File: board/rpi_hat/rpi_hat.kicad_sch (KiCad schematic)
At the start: 9 parts, among them J1 DB9_Male, J2 DB9_Male, J3 Raspberry_Pi_2_3

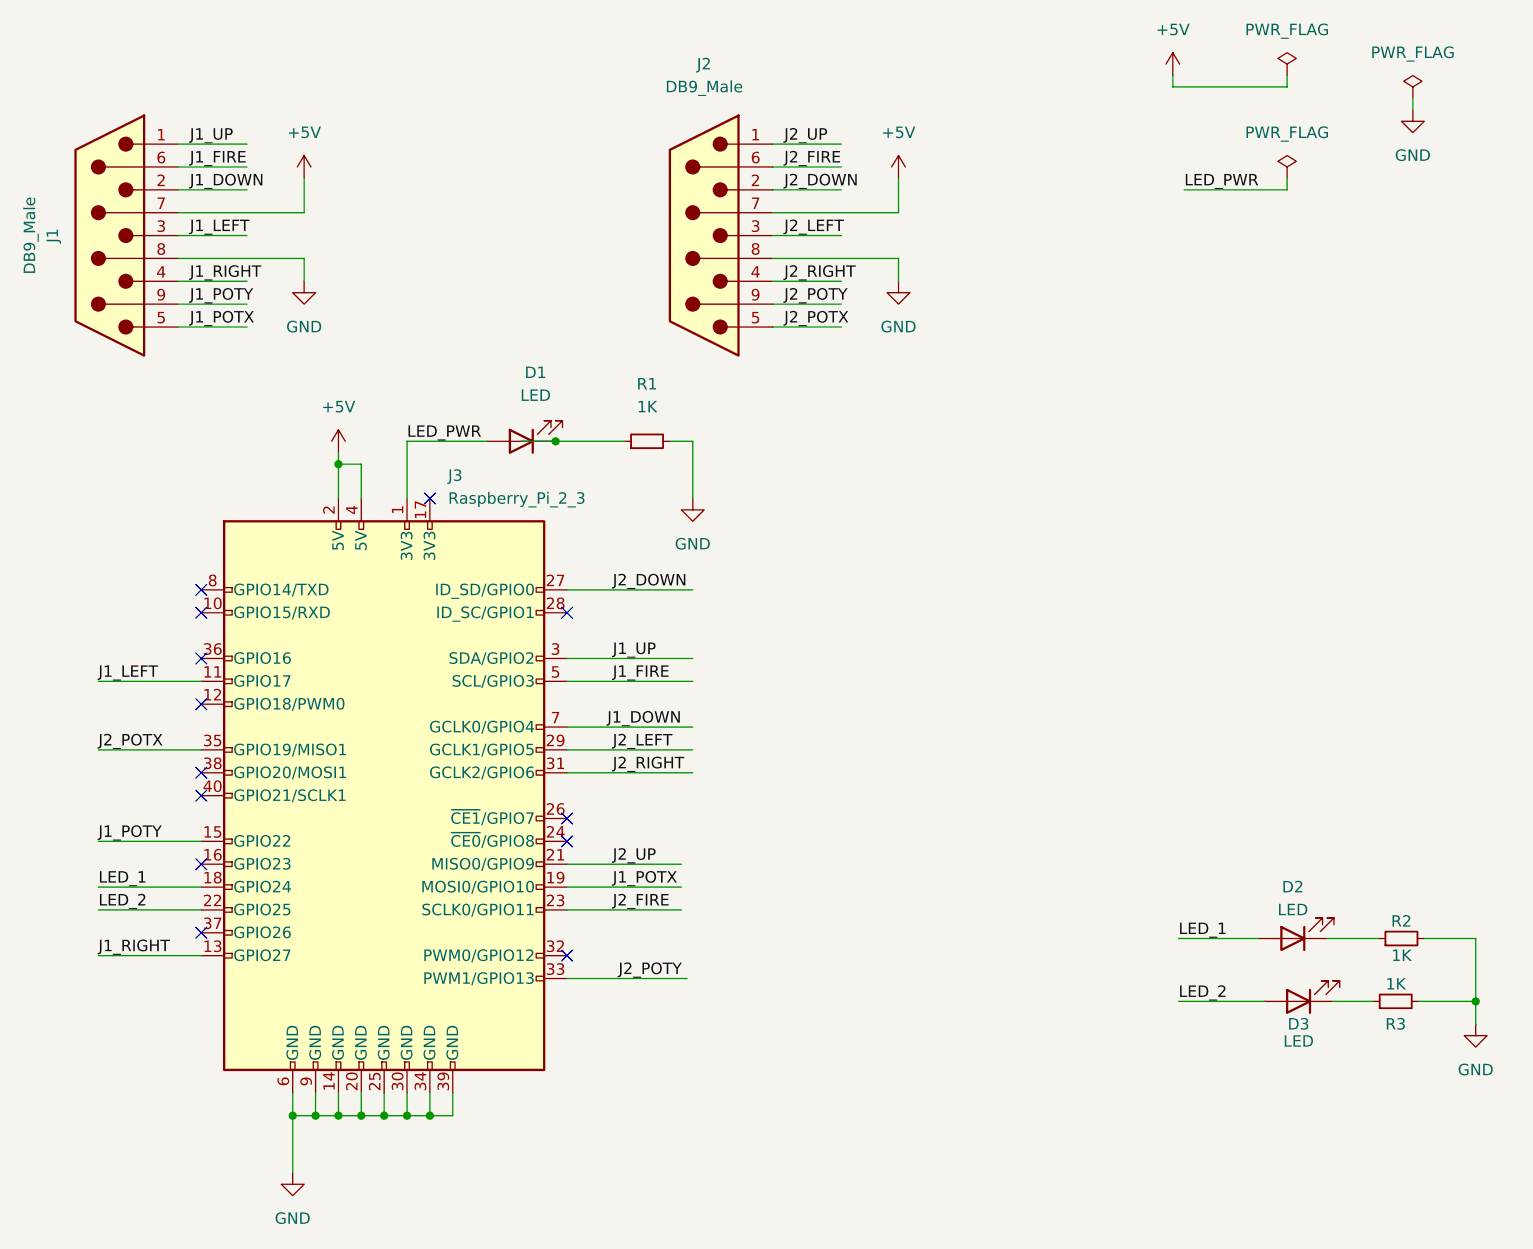
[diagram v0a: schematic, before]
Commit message: rpi hat: rev A
Routing re done to make it easier to use
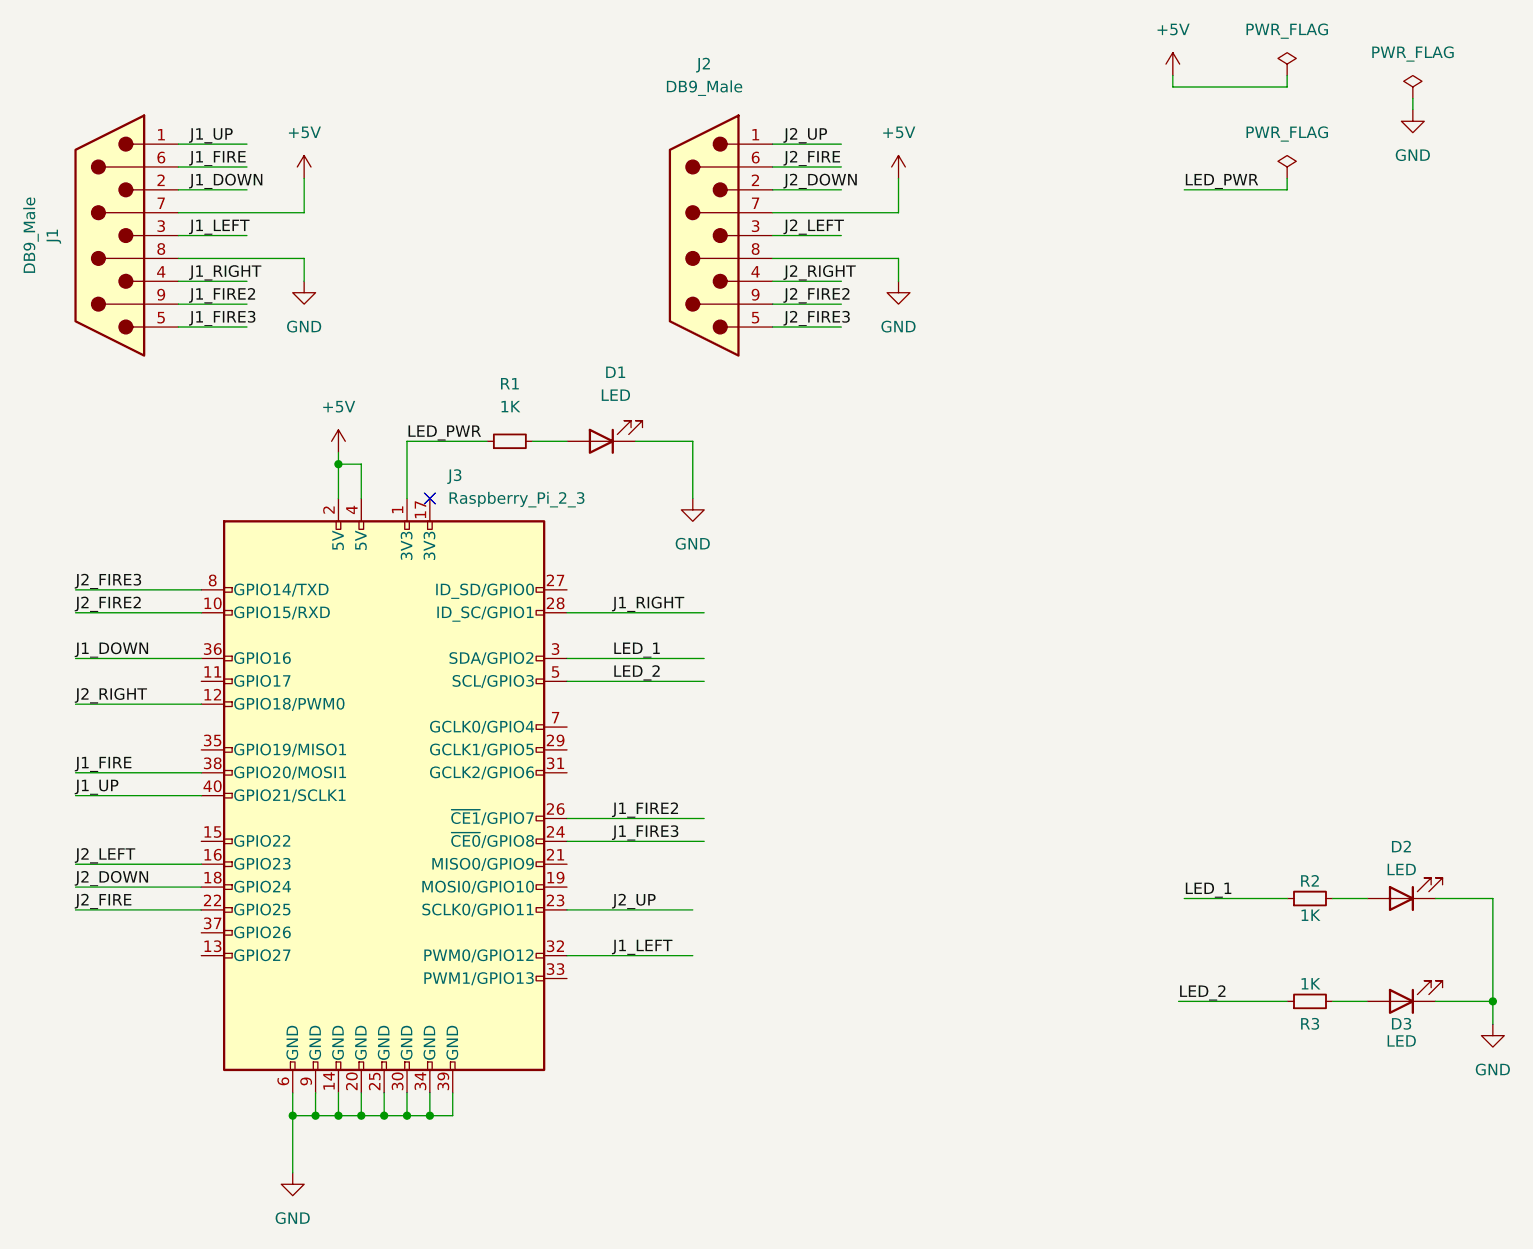
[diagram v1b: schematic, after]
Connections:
- net GND: now also D1.1 (K), D2.1 (K), D3.1 (K); no longer R1.2, R2.2, R3.2
- net J1_DOWN: now also J3.36 (GPIO16); no longer J3.7 (GCLK0/GPIO4)
- net J1_FIRE: now also J3.38 (GPIO20/MOSI1); no longer J3.5 (SCL/GPIO3)
- net J1_LEFT: now also J3.32 (PWM0/GPIO12); no longer J3.11 (GPIO17)
- net J1_RIGHT: now also J3.28 (ID_SC/GPIO1); no longer J3.13 (GPIO27)
- net J1_UP: now also J3.40 (GPIO21/SCLK1); no longer J3.3 (SDA/GPIO2)
- net J2_DOWN: now also J3.18 (GPIO24); no longer J3.27 (ID_SD/GPIO0)
- net J2_FIRE: now also J3.22 (GPIO25); no longer J3.23 (SCLK0/GPIO11)
- net J2_LEFT: now also J3.16 (GPIO23); no longer J3.29 (GCLK1/GPIO5)
- net J2_RIGHT: now also J3.12 (GPIO18/PWM0); no longer J3.31 (GCLK2/GPIO6)
- net J2_UP: now also J3.23 (SCLK0/GPIO11); no longer J3.21 (MISO0/GPIO9)
- net LED_1: now also J3.3 (SDA/GPIO2), R2.1; no longer D2.2 (A), J3.18 (GPIO24)
- net LED_2: now also J3.5 (SCL/GPIO3), R3.1; no longer D3.2 (A), J3.22 (GPIO25)
- net LED_PWR: now also R1.1; no longer D1.2 (A)
- net J2_FIRE2: now reaches J3.10 (GPIO15/RXD)
- net J2_FIRE2: now also J2.9
- net J1_FIRE3: now reaches J3.24 (~{CE0}/GPIO8)
- net J1_FIRE3: now also J1.5
- net J1_FIRE2: now reaches J3.26 (~{CE1}/GPIO7)
- net J1_FIRE2: now also J1.9
- net J2_FIRE3: now reaches J3.8 (GPIO14/TXD)
- net J2_FIRE3: now also J2.5
- net J1_POTX: no longer names the net of J3.19 (MOSI0/GPIO10)
- net J1_POTX: no longer J1.5
- net J1_POTY: no longer names the net of J3.15 (GPIO22)
- net J1_POTY: no longer J1.9
- net J2_POTX: no longer names the net of J3.35 (GPIO19/MISO1)
- net J2_POTX: no longer J2.5
- net J2_POTY: no longer names the net of J3.33 (PWM1/GPIO13)
- net J2_POTY: no longer J2.9
- new net: D1.2 (A), R1.2
- new net: D3.2 (A), R3.2
- new net: D2.2 (A), R2.2
- no-connect marks 13 -> 1
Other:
- company: (none) -> Ricardo Quesada
- title: (none) -> Unijoysticle Tester
- moved on the sheet: D1, D2, D3, R1, R2, R3

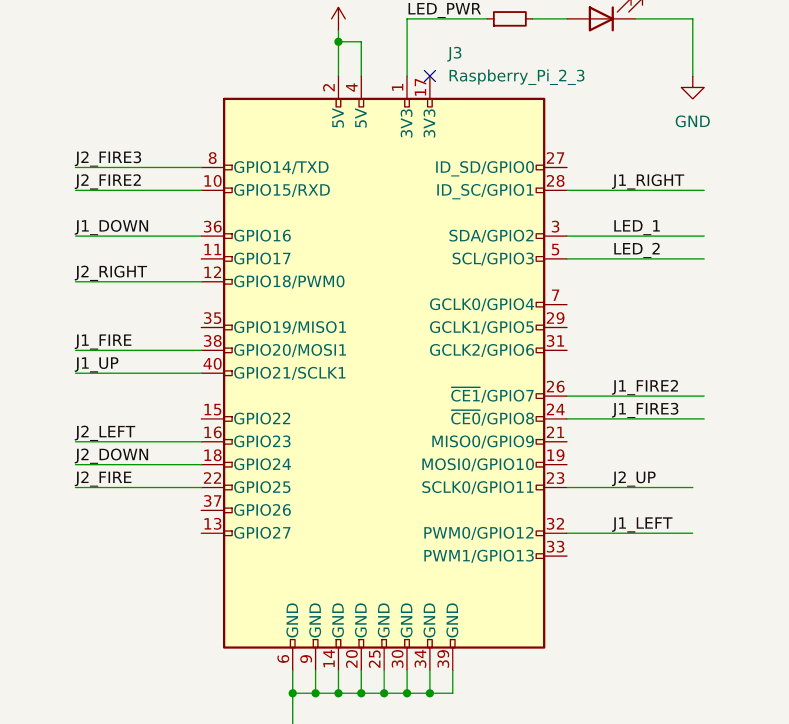
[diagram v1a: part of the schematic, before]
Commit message: rpi_hat: migrated to kicad 7
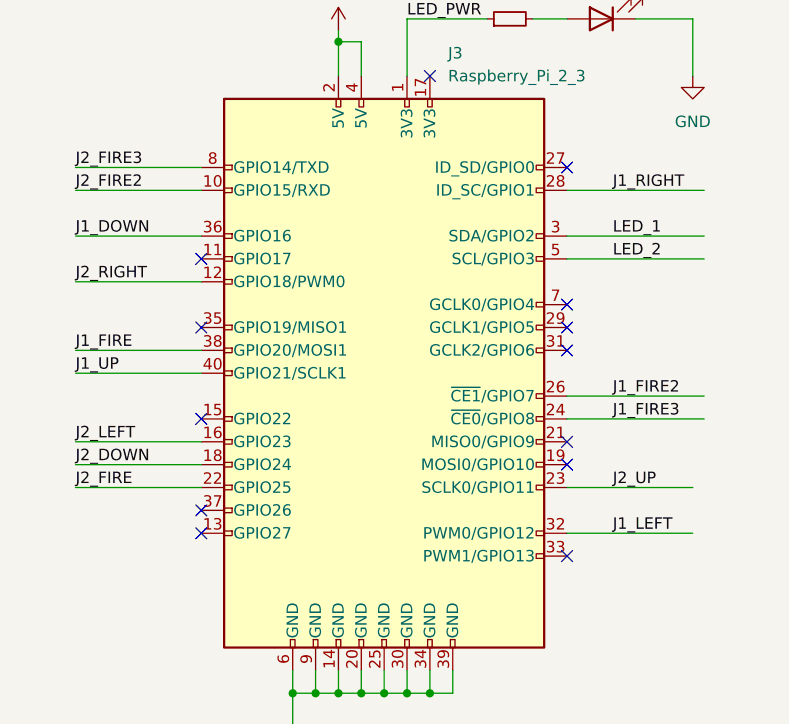
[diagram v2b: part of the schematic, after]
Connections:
- no-connect marks 1 -> 13
